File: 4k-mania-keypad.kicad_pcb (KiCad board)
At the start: 2 copper layers, 112 x 47.2 mm, 49 parts, among them J1 USB_C_Receptacle_USB2.0, J4 Conn_01x03, J5 Conn_01x03, J6 Conn_01x03, J7 Conn_01x03, SW1 RotaryEncoder_Switch, SW2 RotaryEncoder_Switch, SW3 SW_Push, U1 AP2112K-3.3, U2 RP2040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

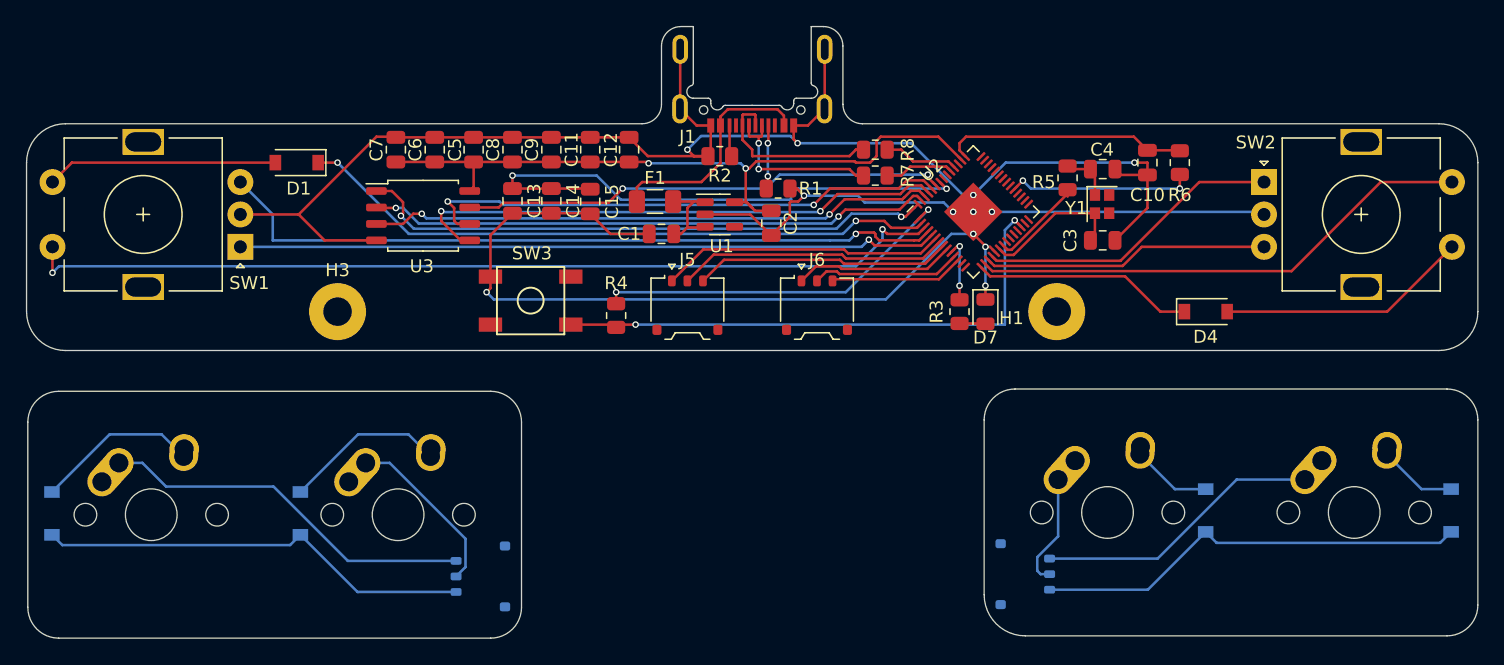
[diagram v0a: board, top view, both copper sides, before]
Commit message: usb routing fix
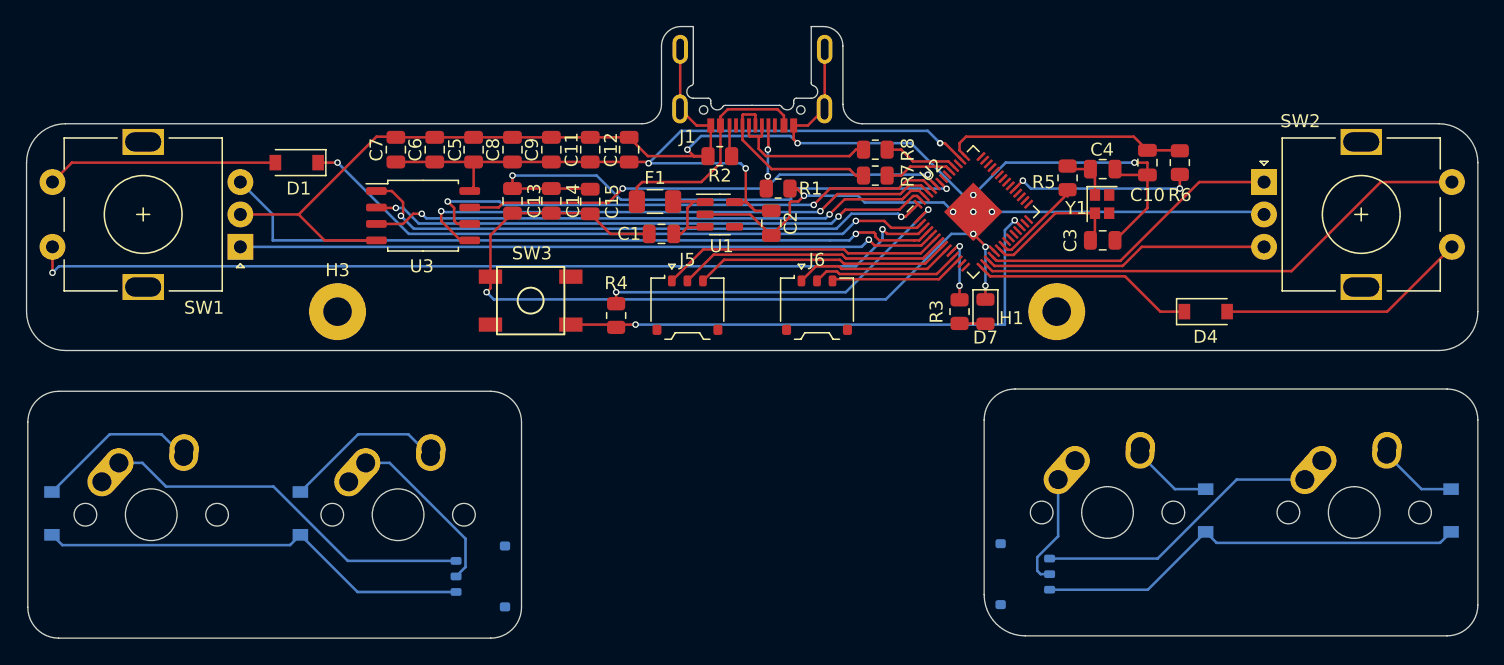
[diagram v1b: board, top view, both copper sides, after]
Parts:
- J4, J5, J6, J7: footprint project_various:Molex_Pico-EZmate_78171-0003_1x03-1MP_P1.20mm_Vertical -> Connector_Molex:Molex_Pico-EZmate_78171-0003_1x03-1MP_P1.20mm_Vertical
- SW1, SW2: footprint project_various:RotaryEncoder_Alps_EC11E-Switch_Vertical_H20mm -> Rotary_Encoder:RotaryEncoder_Alps_EC11E-Switch_Vertical_H20mm
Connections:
- J1 pad A6: RP_DM -> RP_DP
- J1 pad A7: RP_DP -> RP_DM
- J1 pad B6: RP_DM -> RP_DP
- J1 pad B7: RP_DP -> RP_DM
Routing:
- net +3.3V: track 103.3 -> 110.3 mm, vias 8 -> 9
- net RP_DM: track 14.1 -> 12.2 mm
- net RP_DP: track 13.5 -> 14.2 mm, vias 2 -> 0
- net Net-(J1-CC1): track 4.93 -> 5.43 mm
